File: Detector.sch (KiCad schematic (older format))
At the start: 23 parts, among them Q1 BC557, T1 TRANSFO2, U1 LM311N, U2 H11L1, U3 7805

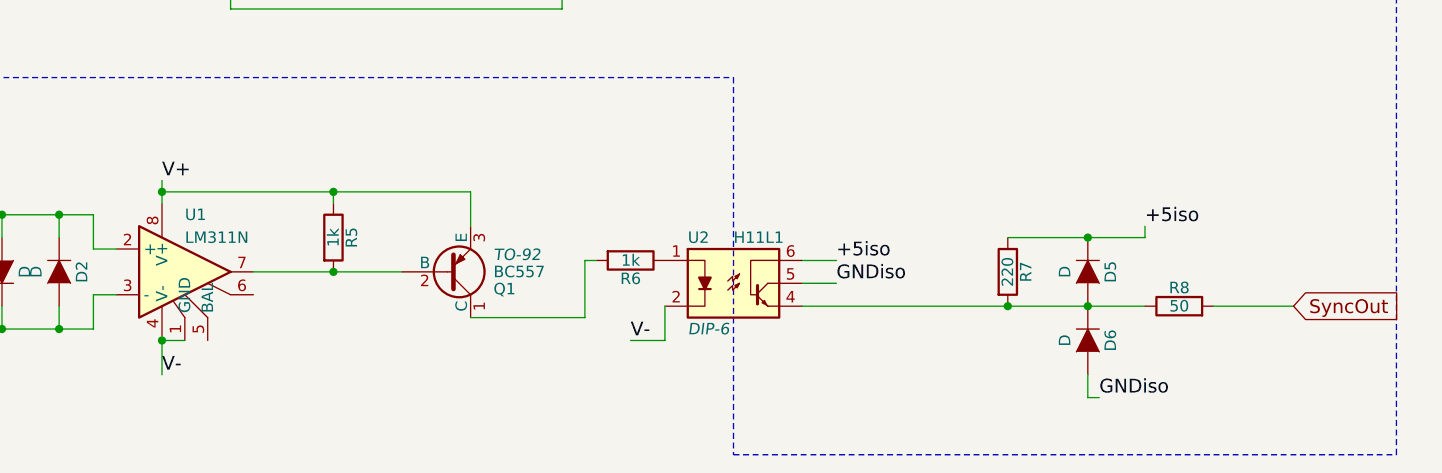
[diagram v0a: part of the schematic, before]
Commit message: Simplified, and added datasheets.
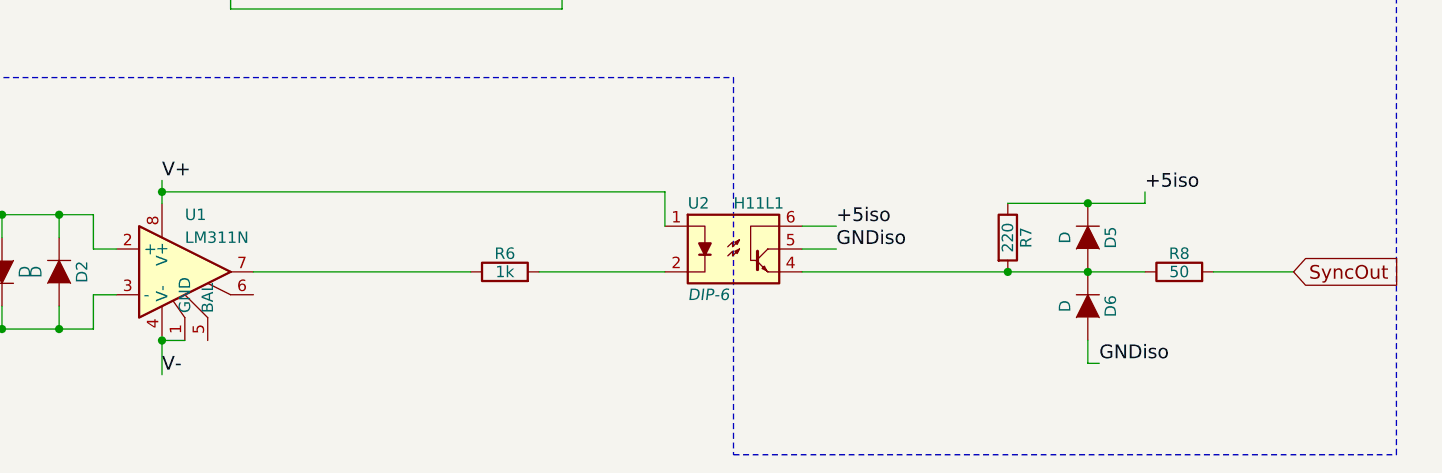
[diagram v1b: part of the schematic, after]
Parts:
- removed Q1: BC557, TO-92, symbol BC557
- removed R5: 1k, symbol R
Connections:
- net V+: now also U2.1
- net V-: no longer U2.2
- net at U1.7: now also R6.1
- net at R6.2: now also U2.2
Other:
- moved on the sheet: D5, D6, R6, R7, R8, U2
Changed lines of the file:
@@
 Title "Mains Synchronization Pulse Generator"
 Date "2016-04-14"
-Rev "0.1"
+Rev "0.2"
 Comp "Kjaergaard Lab, University of Otago"
 Comment1 "Matthew Chilcott"
@@
 L 4N26 U2
 U 1 1 570EC519
-P 6700 4800
-F 0 "U2" H 6500 5000 50  0000 L CNN
-F 1 "H11L1" H 6700 5000 50  0000 L CNN
-F 2 "DIP-6" H 6500 4600 50  0000 L CIN
-F 3 "" H 6700 4800 50  0000 L CNN
-	1    6700 4800
-	1    0    0    -1
-$EndComp
-$Comp
-L BC557 Q1
-U 1 1 570EC70F
-P 5450 4750
-F 0 "Q1" H 5650 4825 50  0000 L CNN
-F 1 "BC557" H 5650 4750 50  0000 L CNN
-F 2 "TO-92" H 5650 4675 50  0000 L CIN
-F 3 "" H 5450 4750 50  0000 L CNN
-	1    5450 4750
-	1    0    0    1
+P 6700 4650
+F 0 "U2" H 6500 4850 50  0000 L CNN
+F 1 "H11L1" H 6700 4850 50  0000 L CNN
+F 2 "DIP-6" H 6500 4450 50  0000 L CIN
+F 3 "" H 6700 4650 50  0000 L CNN
+	1    6700 4650
+	1    0    0    -1
 $EndComp
 $Comp
@@
 Text Label 4200 4350 0    60   ~ 0
 V+
-$Comp
-L R R5
-U 1 1 570ED0F7
-P 4950 4600
-F 0 "R5" V 5030 4600 50  0000 C CNN
-F 1 "1k" V 4950 4600 50  0000 C CNN
-F 2 "" V 4880 4600 50  0000 C CNN
-F 3 "" H 4950 4600 50  0000 C CNN
-	1    4950 4600
-	1    0    0    -1
-$EndComp
 Wire Wire Line
 	2400 5000 3900 5000
@@
 	4200 4350 4200 4450
 Wire Wire Line
-	4600 4750 5250 4750
-Wire Wire Line
-	4200 4400 5550 4400
-Wire Wire Line
-	4950 4400 4950 4450
+	4200 4400 6400 4400
 Connection ~ 4200 4400
-Connection ~ 4950 4750
 Connection ~ 4200 5050
 Connection ~ 3150 5000
-Connection ~ 4950 4400
-Wire Wire Line
-	5550 4400 5550 4550
 $Comp
 L R R6
 U 1 1 570ED540
-P 6250 4700
-F 0 "R6" V 6330 4700 50  0000 C CNN
-F 1 "1k" V 6250 4700 50  0000 C CNN
-F 2 "" V 6180 4700 50  0000 C CNN
-F 3 "" H 6250 4700 50  0000 C CNN
-	1    6250 4700
-	0    1    1    0
-$EndComp
-Text Label 6250 5050 0    60   ~ 0
-V-
-Wire Wire Line
-	6400 4900 6400 5050
-Wire Wire Line
-	6400 5050 6250 5050
-Wire Wire Line
-	5550 4950 6050 4950
-Wire Wire Line
-	6050 4950 6050 4700
-Wire Wire Line
-	6050 4700 6100 4700
+P 5700 4750
+F 0 "R6" V 5780 4750 50  0000 C CNN
+F 1 "1k" V 5700 4750 50  0000 C CNN
+F 2 "" V 5630 4750 50  0000 C CNN
+F 3 "" H 5700 4750 50  0000 C CNN
+	1    5700 4750
+	0    -1   -1   0
+$EndComp
 Wire Wire Line
 	2000 2800 2350 2800
@@
 Connection ~ 8100 3300
 Connection ~ 8100 3000
-Text Label 7150 4700 0    60   ~ 0
+Text Label 7150 4550 0    60   ~ 0
 +5iso
-Text Label 7150 4800 0    60   ~ 0
+Text Label 7150 4650 0    60   ~ 0
 GNDiso
 Wire Wire Line
-	7150 4700 7000 4700
-Wire Wire Line
-	7000 4800 7150 4800
+	7150 4550 7000 4550
+Wire Wire Line
+	7000 4650 7150 4650
 $Comp
 L R R7
 U 1 1 570F0A38
-P 7900 4750
-F 0 "R7" V 7980 4750 50  0000 C CNN
-F 1 "220" V 7900 4750 50  0000 C CNN
-F 2 "" V 7830 4750 50  0000 C CNN
-F 3 "" H 7900 4750 50  0000 C CNN
-	1    7900 4750
+P 7900 4600
+F 0 "R7" V 7980 4600 50  0000 C CNN
+F 1 "220" V 7900 4600 50  0000 C CNN
+F 2 "" V 7830 4600 50  0000 C CNN
+F 3 "" H 7900 4600 50  0000 C CNN
+	1    7900 4600
 	1    0    0    -1
 $EndComp
@@
 L D D5
 U 1 1 570F0A97
-P 8250 4750
-F 0 "D5" H 8250 4850 50  0000 C CNN
-F 1 "D" H 8250 4650 50  0000 C CNN
-F 2 "" H 8250 4750 50  0000 C CNN
-F 3 "" H 8250 4750 50  0000 C CNN
-	1    8250 4750
+P 8250 4600
+F 0 "D5" H 8250 4700 50  0000 C CNN
+F 1 "D" H 8250 4500 50  0000 C CNN
+F 2 "" H 8250 4600 50  0000 C CNN
+F 3 "" H 8250 4600 50  0000 C CNN
+	1    8250 4600
 	0    1    1    0
 $EndComp
@@
 L D D6
 U 1 1 570F0AF0
-P 8250 5050
-F 0 "D6" H 8250 5150 50  0000 C CNN
-F 1 "D" H 8250 4950 50  0000 C CNN
-F 2 "" H 8250 5050 50  0000 C CNN
-F 3 "" H 8250 5050 50  0000 C CNN
-	1    8250 5050
+P 8250 4900
+F 0 "D6" H 8250 5000 50  0000 C CNN
+F 1 "D" H 8250 4800 50  0000 C CNN
+F 2 "" H 8250 4900 50  0000 C CNN
+F 3 "" H 8250 4900 50  0000 C CNN
+	1    8250 4900
 	0    1    1    0
 $EndComp
@@
 L R R8
 U 1 1 570F0B67
-P 8650 4900
-F 0 "R8" V 8730 4900 50  0000 C CNN
-F 1 "50" V 8650 4900 50  0000 C CNN
-F 2 "" V 8580 4900 50  0000 C CNN
-F 3 "" H 8650 4900 50  0000 C CNN
-	1    8650 4900
+P 8650 4750
+F 0 "R8" V 8730 4750 50  0000 C CNN
+F 1 "50" V 8650 4750 50  0000 C CNN
+F 2 "" V 8580 4750 50  0000 C CNN
+F 3 "" H 8650 4750 50  0000 C CNN
+	1    8650 4750
 	0    -1   -1   0
 $EndComp
 Wire Wire Line
-	7000 4900 8500 4900
-Connection ~ 8250 4900
-Connection ~ 7900 4900
-Text Label 8500 4550 0    60   ~ 0
+	7000 4750 8500 4750
+Connection ~ 8250 4750
+Connection ~ 7900 4750
+Text Label 8500 4400 0    60   ~ 0
 +5iso
 Wire Wire Line
-	7900 4600 8500 4600
-Wire Wire Line
-	8500 4600 8500 4550
-Connection ~ 8250 4600
-Text Label 8300 5300 0    60   ~ 0
+	7900 4450 8500 4450
+Wire Wire Line
+	8500 4450 8500 4400
+Connection ~ 8250 4450
+Text Label 8300 5150 0    60   ~ 0
 GNDiso
 Wire Wire Line
-	8300 5300 8250 5300
-Wire Wire Line
-	8250 5300 8250 5200
-Text GLabel 9150 4900 2    60   Input ~ 0
+	8300 5150 8250 5150
+Wire Wire Line
+	8250 5150 8250 5050
+Text GLabel 9150 4750 2    60   Input ~ 0
 SyncOut
 Wire Wire Line
-	9150 4900 8800 4900
+	9150 4750 8800 4750
 Text GLabel 2000 2400 0    60   Input ~ 0
 Phase
@@
 Text Notes 2100 2650 0    60   ~ 0
 240 Vrms
+Wire Wire Line
+	6400 4400 6400 4550
+Wire Wire Line
+	6400 4750 5850 4750
+Wire Wire Line
+	5550 4750 4600 4750
 $EndSCHEMATC
